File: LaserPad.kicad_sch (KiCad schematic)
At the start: 7 parts, among them U1 STM32F072CBTx, U3 PRTR5V0U2X, U4 USBLC6-2SC6

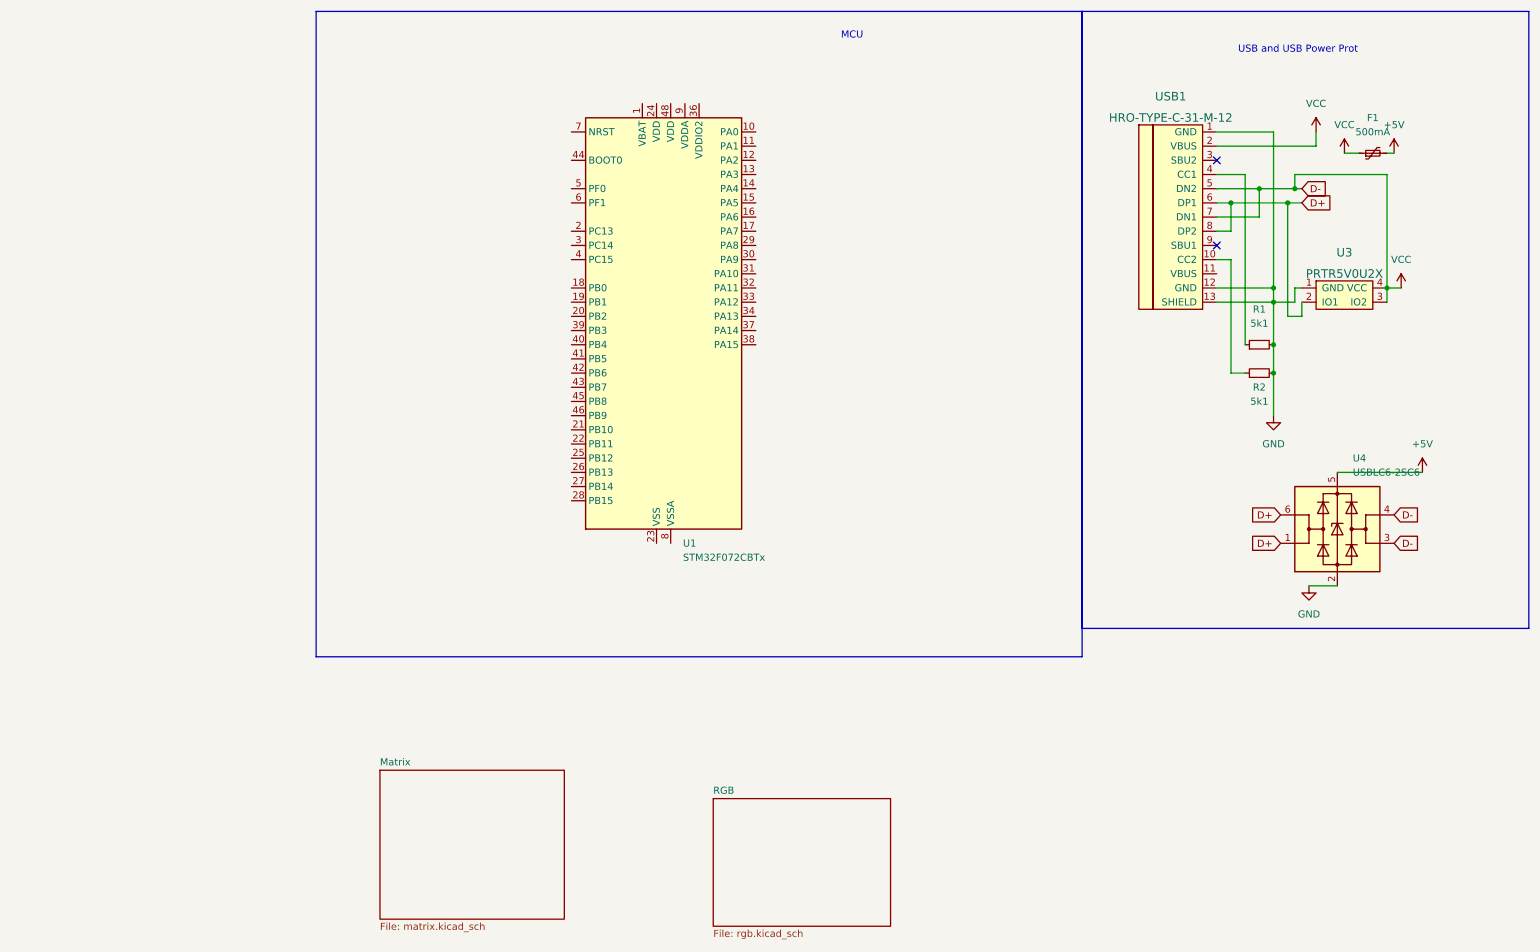
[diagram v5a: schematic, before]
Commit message: Changed MCU to STM32, Redone footprints for USB, keyswitches, LEDS, and other things, and configured PCB Editor for general switch placement
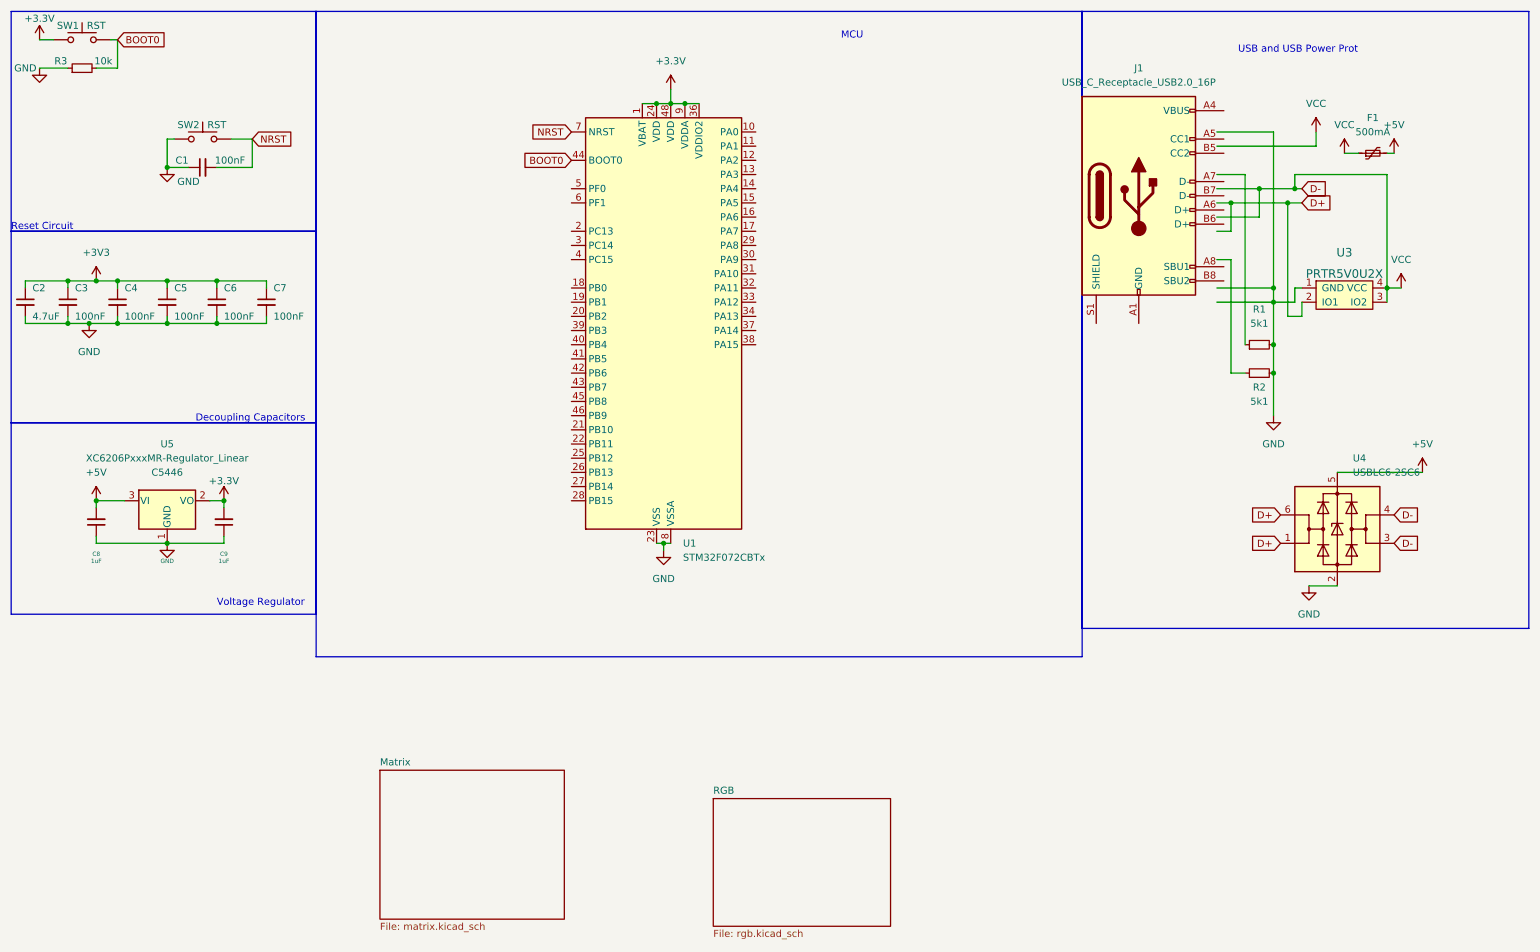
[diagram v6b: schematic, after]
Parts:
- removed USB1: HRO-TYPE-C-31-M-12, symbol Type-C:HRO-TYPE-C-31-M-12
- added C1, C3, C4, C5, C6, C7: 100nF, Capacitor_SMD:C_0402_1005Metric, symbol Device:C_Small
- added C2: 4.7uF, Capacitor_SMD:C_0402_1005Metric, symbol Device:C_Small
- added C8, C9: 1uF, Capacitor_SMD:C_0402_1005Metric, symbol Device:C_Small
- added J1: USB_C_Receptacle_USB2.0_16P, symbol Connector:USB_C_Receptacle_USB2.0_16P
- added R3: 10k, Resistor_SMD:R_0402_1005Metric, symbol Device:R_Small
- added SW1, SW2: RST, Button_Switch_SMD:SW_SPST_SKQG_WithoutStem, symbol Switch:SW_Push
- added U5: XC6206PxxxMR-Regulator_Linear, Package_TO_SOT_SMD:SOT-23, symbol kicad-keyboard-parts:XC6206PxxxMR-Regulator_Linear
- F1: footprint (none) -> Fuse:Fuse_1206_3216Metric
- R1, R2: footprint (none) -> Resistor_SMD:R_0402_1005Metric
- U3: footprint (none) -> random-keyboard-parts:SOT143B
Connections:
- net +5V: now also C8.2, U5.3 (VI)
- net GND: now also U1.23 (VSS), U1.35 (VSS), U1.47 (VSS), U1.8 (VSSA), C1.1, C2.2, C3.2, C4.2, C5.2, C6.2, C7.2, C8.1, C9.1, R3.1, SW2.1, U5.1 (GND)
- net +3.3V: now reaches U1.1 (VBAT)
- net +3.3V: now also U1.24 (VDD), U1.36 (VDDIO2), U1.48 (VDD), U1.9 (VDDA), C9.2, SW1.1, U5.2 (VO)
- net BOOT0: now reaches U1.44 (BOOT0)
- net BOOT0: now also R3.2, SW1.2
- net NRST: now reaches U1.7 (NRST)
- net NRST: now also C1.2, SW2.2
- new net: J1.A1 (GND), J1.A12 (GND), J1.B1 (GND), J1.B12 (GND)
- new net: J1.A4 (VBUS), J1.A9 (VBUS), J1.B4 (VBUS), J1.B9 (VBUS)
- new net +3V3: C2.1, C3.1, C4.1, C5.1, C6.1, C7.1
- no-connect marks 2 -> 0
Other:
- note added: "Decoupling Capacitors"
- note added: "Reset Circuit"
- note added: "Voltage Regulator"

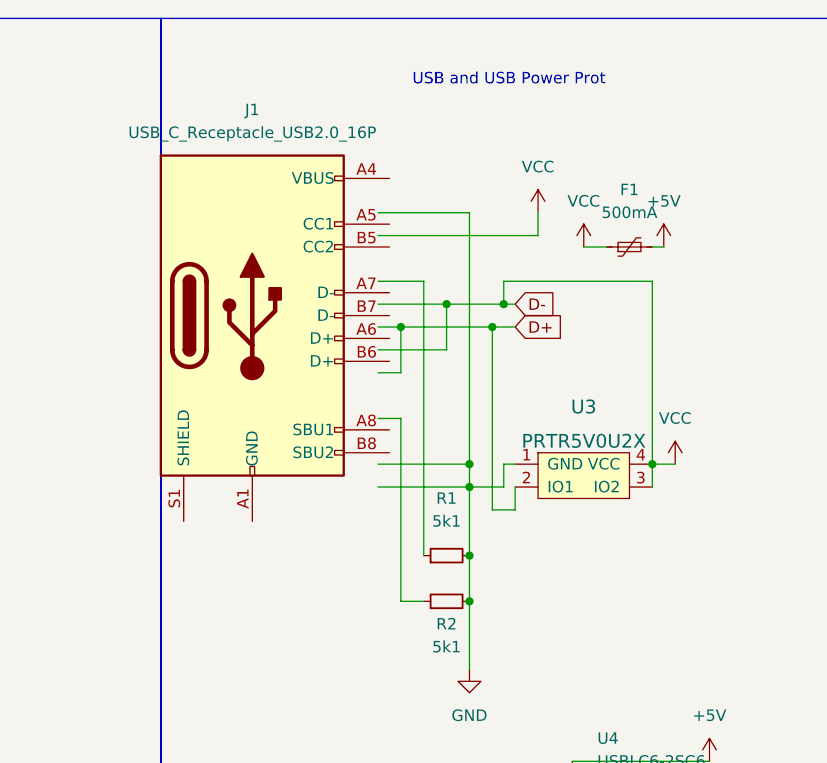
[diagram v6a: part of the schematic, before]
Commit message: updated pcb files, wired up a new usb connector in the schematic, cleaned up a couple of wiring within the schematic
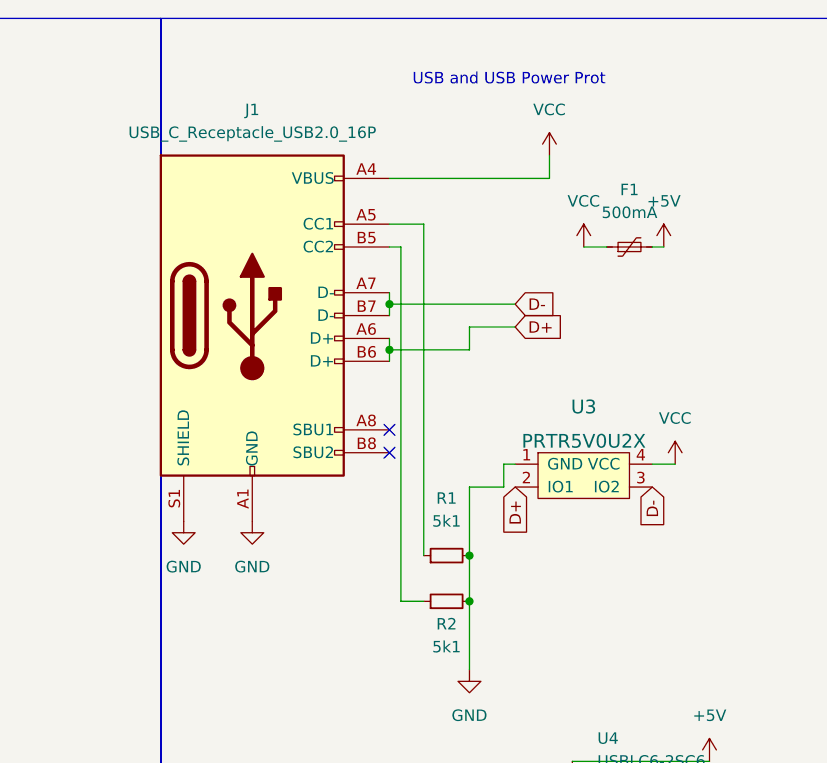
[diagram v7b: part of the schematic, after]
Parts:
- J1: footprint (none) -> Connector_USB:USB_C_Receptacle_HRO_TYPE-C-31-M-12
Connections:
- net D+: now also J1.A6 (D+), J1.B6 (D+)
- net GND: now also J1.A1 (GND), J1.A12 (GND), J1.B1 (GND), J1.B12 (GND), J1.S1 (SHIELD)
- net VCC: now also J1.A4 (VBUS), J1.A9 (VBUS), J1.B4 (VBUS), J1.B9 (VBUS); no longer U3.3 (IO2), U4.3 (I/O2), U4.4 (I/O2)
- net at R1.1: now also J1.A5 (CC1)
- net D-: now reaches J1.A7 (D-)
- net D-: now also J1.B7 (D-), U3.3 (IO2), U4.3 (I/O2), U4.4 (I/O2)
- net at J1.B5 (CC2): now also R2.1
- no-connect marks 0 -> 2

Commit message: Placed Components and in the process of routing
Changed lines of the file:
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@@
-    (stroke (width 0) (type default))
-  )
-  (wire (pts (xy 229.87 30.48) (xy 247.65 30.48))
     (stroke (width 0) (type default))
   )
   (wire (pts (xy 128.27 29.21) (xy 130.81 29.21))
+    (stroke (width 0) (type default))
+  )
+  (wire (pts (xy 229.87 30.48) (xy 241.3 30.48))
     (stroke (width 0) (type default))
   )
@@
   (wire (pts (xy 50.8 100.33) (xy 50.8 101.6))
     (stroke (width 0) (type solid))
-  )
-  (wire (pts (xy 247.65 27.94) (xy 247.65 30.48))
-    (stroke (width 0) (type default))
   )
   (wire (pts (xy 130.81 29.21) (xy 133.35 29.21))
@@
         (path "/d1f15120-cbbc-44e4-8f66-361808e417b1"
           (reference "#PWR027") (unit 1)
-        )
-      )
-    )
-  )
-  (symbol (lib_id "power:VCC") (at 247.65 27.94 0) (unit 1)
-    (in_bom yes) (on_board yes) (dnp no)
-    (property "Reference" "#PWR023" (at 247.65 31.75 0)
-      (effects (font (size 1.27 1.27)) hide)
-    )
-    (property "Value" "VCC" (at 247.65 22.86 0)
-      (effects (font (size 1.27 1.27)))
-    )
-    (property "Footprint" "" (at 247.65 27.94 0)
-      (effects (font (size 1.27 1.27)) hide)
-    )
-    (property "Datasheet" "" (at 247.65 27.94 0)
-      (effects (font (size 1.27 1.27)) hide)
-    )
-    (pin "1")
-    (instances
-      (project "LaserPad"
-        (path "/d1f15120-cbbc-44e4-8f66-361808e417b1"
-          (reference "#PWR023") (unit 1)
         )
       )
@@
         )
       )
+    )
+  )
+  (symbol (lib_id "power:VCC") (at 241.3 30.48 0) (unit 1)
+    (in_bom yes) (on_board yes) (dnp no) (fields_autoplaced)
+    (property "Reference" "#PWR023" (at 241.3 34.29 0)
+      (effects (font (size 1.27 1.27)) hide)
+    )
+    (property "Value" "VCC" (at 241.3 25.4 0)
+      (effects (font (size 1.27 1.27)))
+    )
+    (property "Footprint" "" (at 241.3 30.48 0)
+      (effects (font (size 1.27 1.27)) hide)
+    )
+    (property "Datasheet" "" (at 241.3 30.48 0)
+      (effects (font (size 1.27 1.27)) hide)
+    )
+    (pin "1")
+    (instances
+      (project "LaserPad"
+        (path "/d1f15120-cbbc-44e4-8f66-361808e417b1"
+          (reference "#PWR023") (unit 1)
+        )
+      )
